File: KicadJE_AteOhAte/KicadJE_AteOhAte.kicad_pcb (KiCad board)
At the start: 2 copper layers, 100 x 100 mm, 201 parts, among them J201 In_Accent, J202 In Gate, J203 Out Tom, J301 PJRAS2X2S01AUX, J302 Conn_01x03, P201 Doepfer_Power_10pin, Q201 MMBT2222A, Q202 MMBT2222A, Q203 MMBT2222A, Q204 MMBT2222A, Q205 MMBT2907A, Q206 MMBT2222A, Q207 MMBT2222A, SW201 Con/Tom, U201 TL072, U202 TL072, U203 TL072, U301 TL072, U302 TL072, U303 TL072

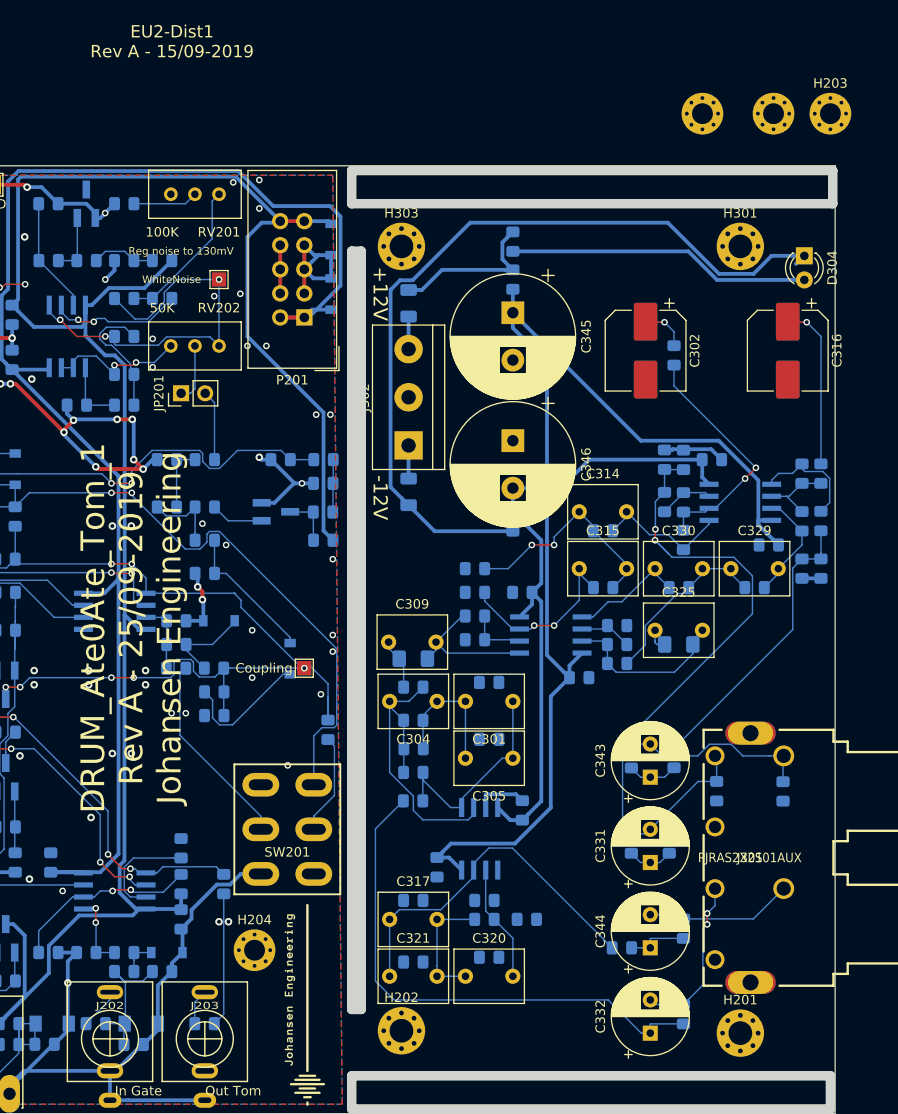
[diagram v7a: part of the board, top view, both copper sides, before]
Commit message: Routing and GND on RIAA
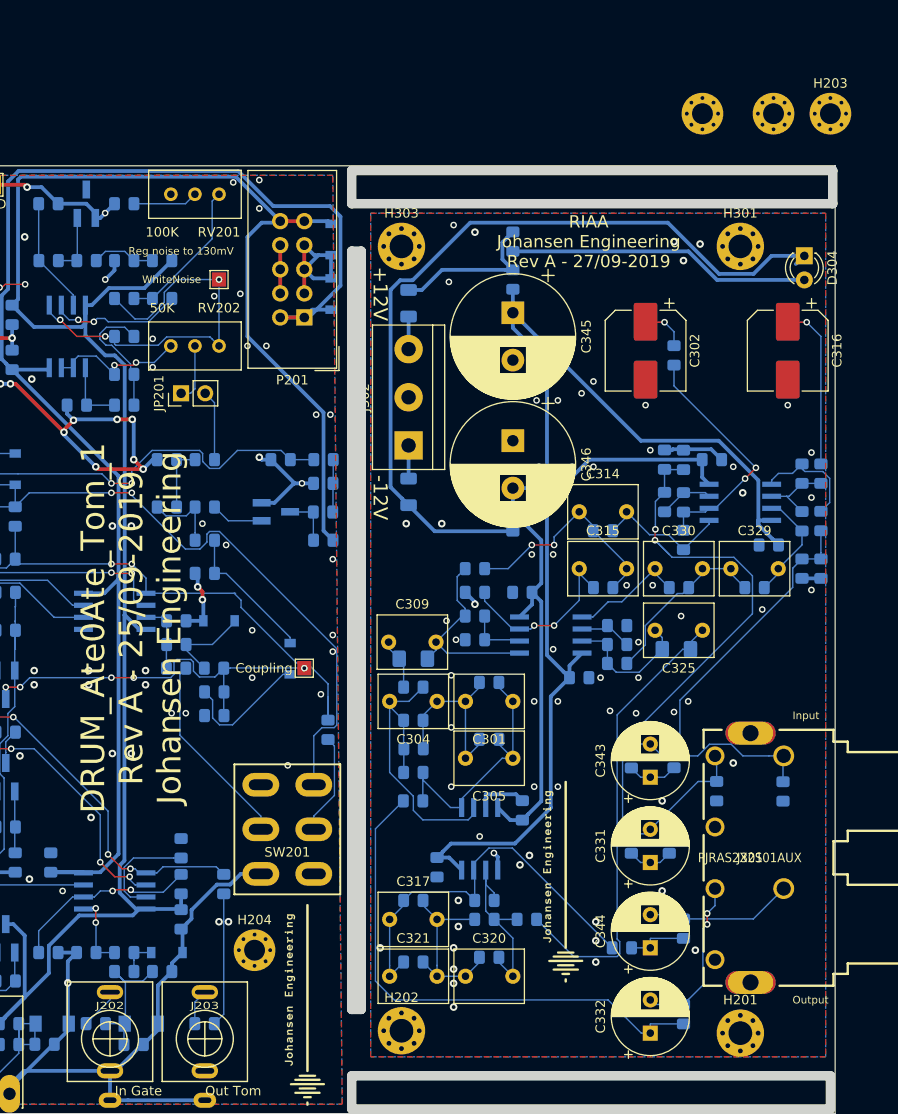
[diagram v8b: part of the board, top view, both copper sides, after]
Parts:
- added G***: LOGO, AJ:Johansen_engineering_logo_25mm_front_neg5, B.Cu at (130.5, 64.5)
- added G***: LOGO, AJ:Johansen_engineering_logo_25mm_front_neg5, F.Cu at (121.5, 125.5)
- moved C325 5.00 mm to (136.0, 99.0), turned to 180 degrees
- moved C326 0.56 mm to (133.2, 101.0), turned to 180 degrees
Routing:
- net Net-(C325-Pad1): track 2.40 -> 49.0 mm
- net Net-(C320-Pad2): track 12.4 -> 21.0 mm
- net Net-(C317-Pad2): track 13.0 -> 20.3 mm
- net L_Rumble_Out: track 15.6 -> 21.3 mm
- net Net-(C301-Pad2): track 14.6 -> 19.8 mm
- net Net-(C301-Pad1): track 23.2 -> 28.4 mm
- net Net-(C317-Pad1): track 37.8 -> 42.6 mm
- net GND: track 212.5 -> 216.2 mm, vias 77 -> 144
- net R_Rumble_Out: track 17.9 -> 14.3 mm
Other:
- board text added: "Input"
- board text added: "Input Gain Stage"
- board text added: "Output"
- board text added: "RIAA"
- board text added: "RIAA Johansen Engineering Rev A - 27/09-2019"
- board text added: "Rumble filter"
- board text removed: "EU2-Dist1 Rev A - 15/09-2019"
- board text removed: "EU2-Dist2 Rev A - 15/09-2019"
